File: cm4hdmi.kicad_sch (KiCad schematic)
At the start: 8 parts, among them J2 2086581051, U5 AP22653FDZ-7, U6 TPD8S009DSMR

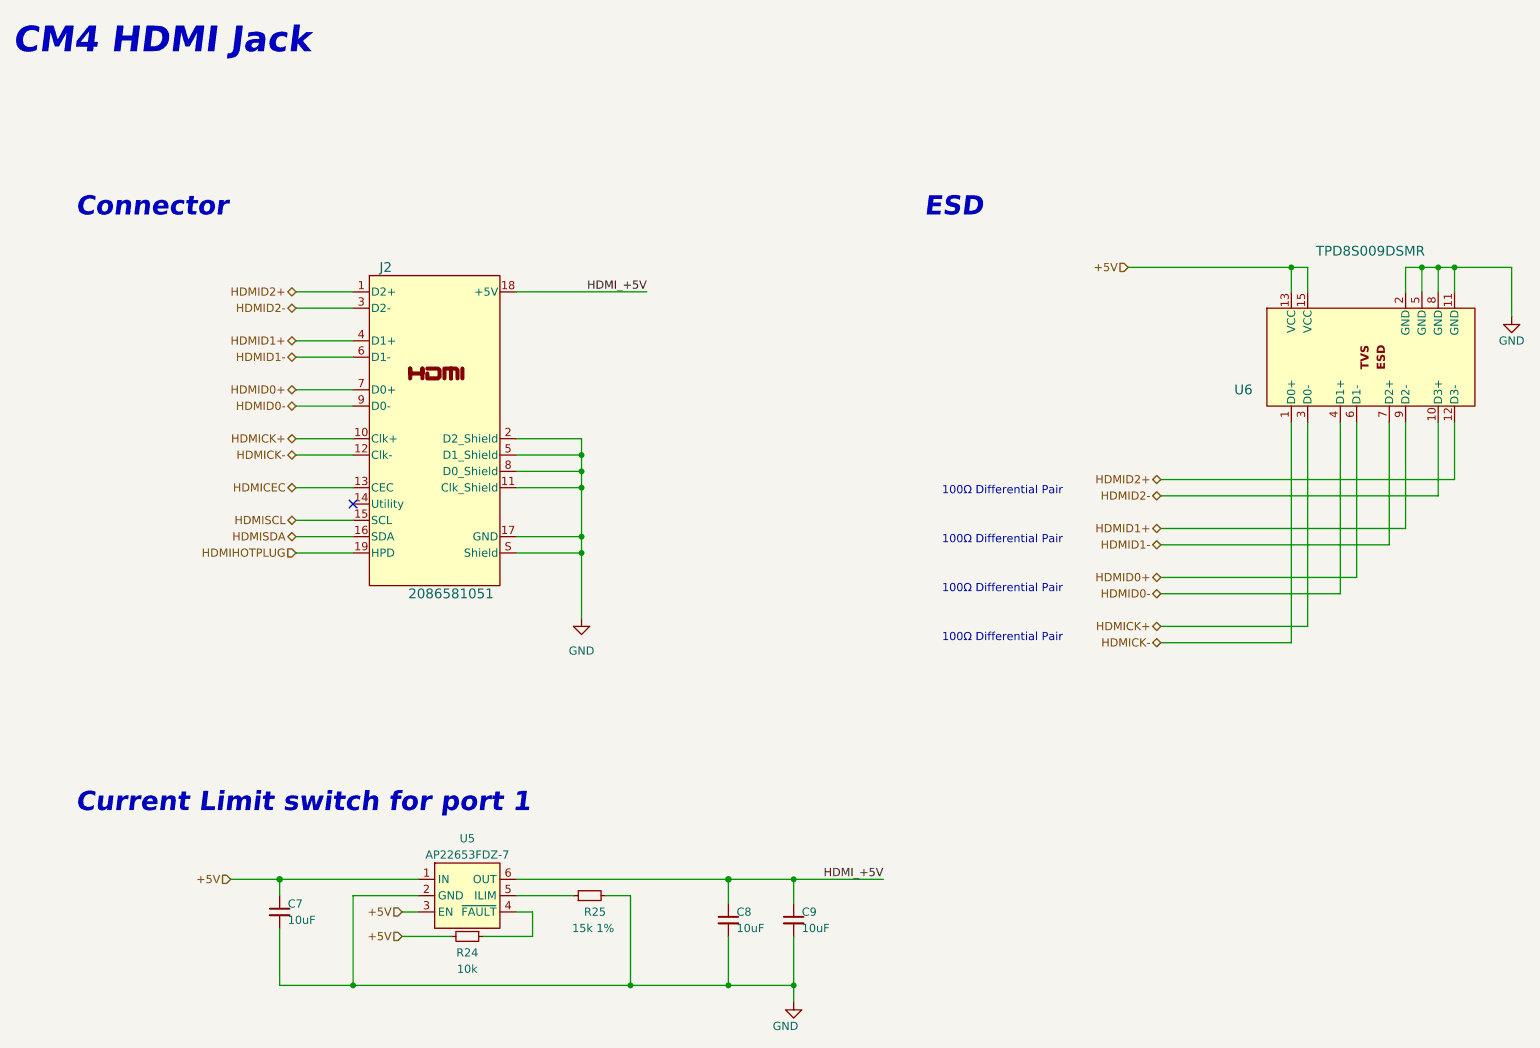
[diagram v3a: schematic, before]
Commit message: initial integration of i2c arbiter
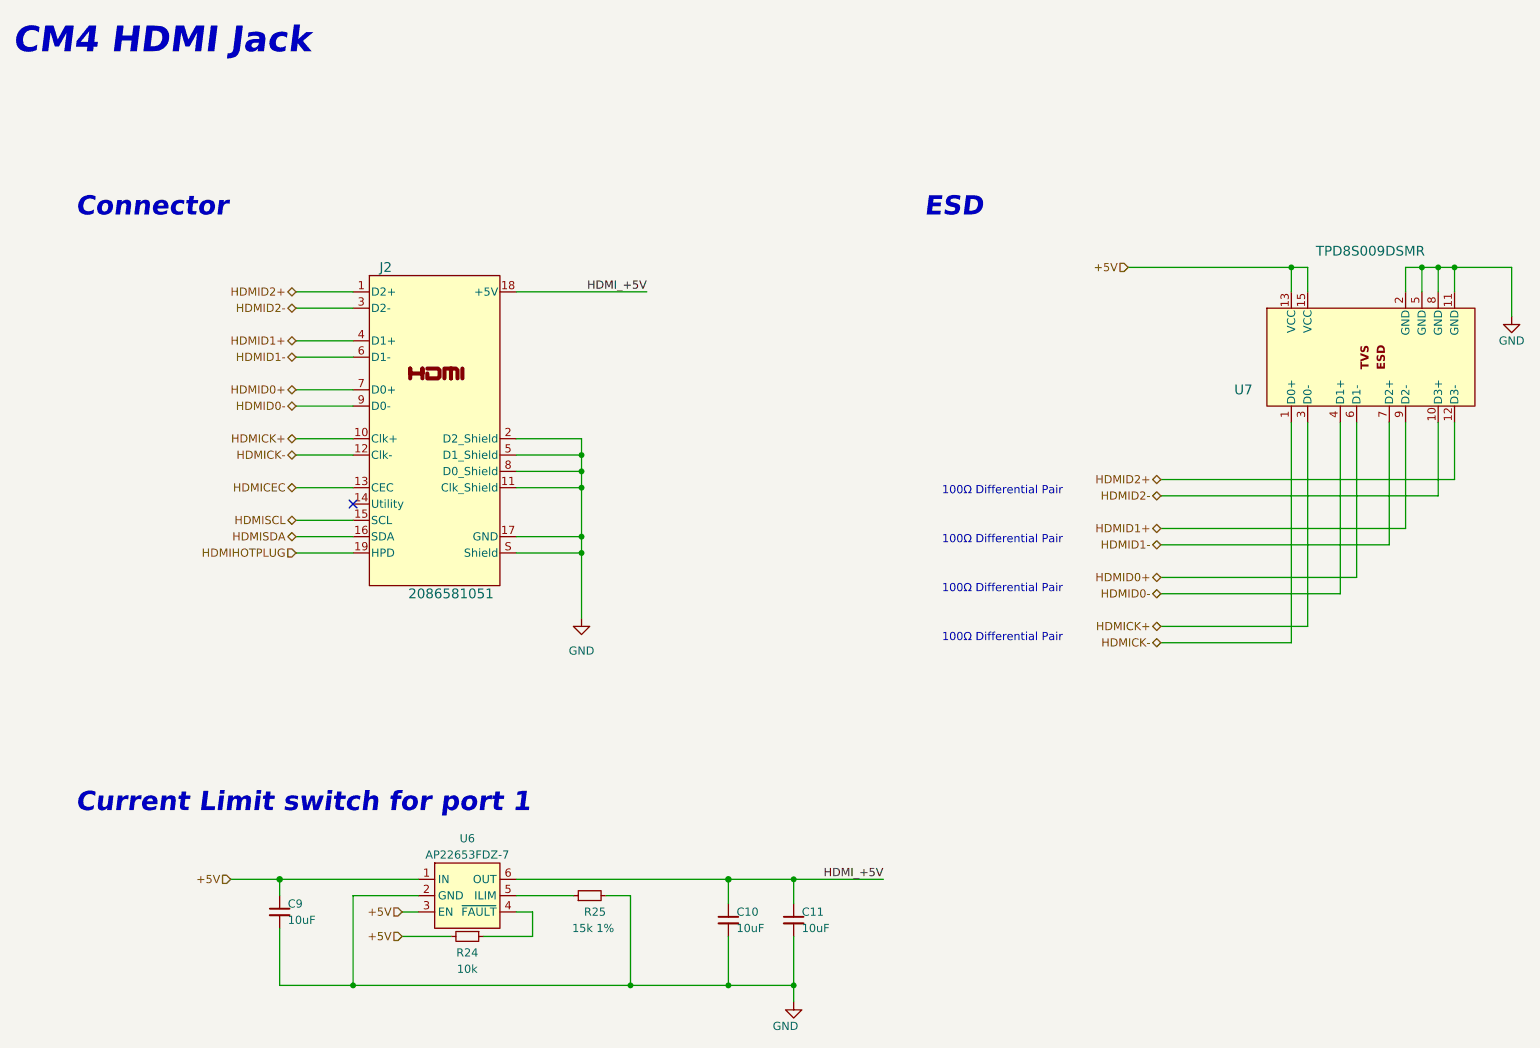
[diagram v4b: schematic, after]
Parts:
- renumbered C8 to C10, C9 to C11, C7 to C9, U5 to U6, U6 to U7
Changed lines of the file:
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@@
   (symbol (lib_id "Power_Protection_Diodes:AP22653FDZ-7") (at 86.36 153.67 0) (unit 1)
     (in_bom yes) (on_board yes)
-    (property "Reference" "U5" (id 0) (at 86.36 144.78 0))
+    (property "Reference" "U6" (id 0) (at 86.36 144.78 0))
     (property "Value" "AP22653FDZ-7" (id 1) (at 86.36 147.32 0))
     (property "Footprint" "Power_Protection_Diodes:Diodes_W-DFN2020-6_A1" (id 2) (at 86.36 167.64 0)
@@
   (symbol (lib_id "Power_Protection_TI:TPD8S009DSMR") (at 227.33 69.85 90) (mirror x) (unit 1)
     (in_bom yes) (on_board yes)
-    (property "Reference" "U6" (id 0) (at 205.74 74.93 90)
+    (property "Reference" "U7" (id 0) (at 205.74 74.93 90)
       (effects (font (size 1.524 1.524)) (justify right))
     )
@@
   (symbol (lib_id "power:GND") (at 104.14 110.49 0) (unit 1)
     (in_bom yes) (on_board yes) (fields_autoplaced)
-    (property "Reference" "#PWR018" (id 0) (at 104.14 116.84 0)
+    (property "Reference" "#PWR019" (id 0) (at 104.14 116.84 0)
       (effects (font (size 1.27 1.27)) hide)
     )
@@
   (symbol (lib_id "power:GND") (at 248.92 63.5 0) (unit 1)
     (in_bom yes) (on_board yes)
-    (property "Reference" "#PWR020" (id 0) (at 248.92 69.85 0)
+    (property "Reference" "#PWR021" (id 0) (at 248.92 69.85 0)
       (effects (font (size 1.27 1.27)) hide)
     )
@@
   (symbol (lib_id "Device:C_Small") (at 137.16 157.48 0) (unit 1)
     (in_bom yes) (on_board yes)
-    (property "Reference" "C9" (id 0) (at 138.43 156.21 0)
+    (property "Reference" "C11" (id 0) (at 138.43 156.21 0)
       (effects (font (size 1.27 1.27)) (justify left))
     )
@@
   (symbol (lib_id "power:GND") (at 137.16 170.18 0) (unit 1)
     (in_bom yes) (on_board yes)
-    (property "Reference" "#PWR019" (id 0) (at 137.16 176.53 0)
+    (property "Reference" "#PWR020" (id 0) (at 137.16 176.53 0)
       (effects (font (size 1.27 1.27)) hide)
     )
@@
   (symbol (lib_id "Device:C_Small") (at 127 157.48 0) (unit 1)
     (in_bom yes) (on_board yes)
-    (property "Reference" "C8" (id 0) (at 128.27 156.21 0)
+    (property "Reference" "C10" (id 0) (at 128.27 156.21 0)
       (effects (font (size 1.27 1.27)) (justify left))
     )
@@
   (symbol (lib_id "Device:C_Small") (at 57.15 156.21 0) (unit 1)
     (in_bom yes) (on_board yes)
-    (property "Reference" "C7" (id 0) (at 58.42 154.94 0)
-      (effects (font (size 1.27 1.27)) (justify left))
-    )
+    (property "Reference" "C9" (id 0) (at 58.42 154.94 0)
+      (effects (font (size 1.27 1.27)) (justify left))
+    )

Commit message: footprint assignment
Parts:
- renumbered C9 to C11, C10 to C12, C11 to C13, R24 to R30, R25 to R31, U6 to U7, U7 to U8
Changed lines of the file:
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@@
   (symbol (lib_id "Power_Protection_Diodes:AP22653FDZ-7") (at 86.36 153.67 0) (unit 1)
     (in_bom yes) (on_board yes)
-    (property "Reference" "U6" (id 0) (at 86.36 144.78 0))
+    (property "Reference" "U7" (id 0) (at 86.36 144.78 0))
     (property "Value" "AP22653FDZ-7" (id 1) (at 86.36 147.32 0))
     (property "Footprint" "Power_Protection_Diodes:Diodes_W-DFN2020-6_A1" (id 2) (at 86.36 167.64 0)
@@
   (symbol (lib_id "Device:R_Small") (at 105.41 153.67 90) (unit 1)
     (in_bom yes) (on_board yes)
-    (property "Reference" "R25" (id 0) (at 107.95 156.21 90)
+    (property "Reference" "R31" (id 0) (at 107.95 156.21 90)
       (effects (font (size 1.27 1.27)) (justify left))
     )
@@
   (symbol (lib_id "Power_Protection_TI:TPD8S009DSMR") (at 227.33 69.85 90) (mirror x) (unit 1)
     (in_bom yes) (on_board yes)
-    (property "Reference" "U7" (id 0) (at 205.74 74.93 90)
+    (property "Reference" "U8" (id 0) (at 205.74 74.93 90)
       (effects (font (size 1.524 1.524)) (justify right))
     )
@@
   (symbol (lib_id "Device:R_Small") (at 86.36 160.02 270) (unit 1)
     (in_bom yes) (on_board yes)
-    (property "Reference" "R24" (id 0) (at 86.36 162.56 90))
+    (property "Reference" "R30" (id 0) (at 86.36 162.56 90))
     (property "Value" "10k" (id 1) (at 86.36 165.1 90))
     (property "Footprint" "Resistor_SMD:R_0402_1005Metric" (id 2) (at 86.36 160.02 0)
@@
   (symbol (lib_id "power:GND") (at 104.14 110.49 0) (unit 1)
     (in_bom yes) (on_board yes) (fields_autoplaced)
-    (property "Reference" "#PWR019" (id 0) (at 104.14 116.84 0)
+    (property "Reference" "#PWR021" (id 0) (at 104.14 116.84 0)
       (effects (font (size 1.27 1.27)) hide)
     )
@@
   (symbol (lib_id "power:GND") (at 248.92 63.5 0) (unit 1)
     (in_bom yes) (on_board yes)
-    (property "Reference" "#PWR021" (id 0) (at 248.92 69.85 0)
+    (property "Reference" "#PWR023" (id 0) (at 248.92 69.85 0)
       (effects (font (size 1.27 1.27)) hide)
     )
@@
   (symbol (lib_id "Device:C_Small") (at 137.16 157.48 0) (unit 1)
     (in_bom yes) (on_board yes)
-    (property "Reference" "C11" (id 0) (at 138.43 156.21 0)
+    (property "Reference" "C13" (id 0) (at 138.43 156.21 0)
       (effects (font (size 1.27 1.27)) (justify left))
     )
@@
   (symbol (lib_id "power:GND") (at 137.16 170.18 0) (unit 1)
     (in_bom yes) (on_board yes)
-    (property "Reference" "#PWR020" (id 0) (at 137.16 176.53 0)
+    (property "Reference" "#PWR022" (id 0) (at 137.16 176.53 0)
       (effects (font (size 1.27 1.27)) hide)
     )
@@
   (symbol (lib_id "Device:C_Small") (at 127 157.48 0) (unit 1)
     (in_bom yes) (on_board yes)
-    (property "Reference" "C10" (id 0) (at 128.27 156.21 0)
+    (property "Reference" "C12" (id 0) (at 128.27 156.21 0)
       (effects (font (size 1.27 1.27)) (justify left))
     )
@@
   (symbol (lib_id "Device:C_Small") (at 57.15 156.21 0) (unit 1)
     (in_bom yes) (on_board yes)
-    (property "Reference" "C9" (id 0) (at 58.42 154.94 0)
-      (effects (font (size 1.27 1.27)) (justify left))
-    )
+    (property "Reference" "C11" (id 0) (at 58.42 154.94 0)
+      (effects (font (size 1.27 1.27)) (justify left))
+    )
